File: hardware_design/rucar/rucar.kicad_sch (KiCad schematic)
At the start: 6 parts

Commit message: finish hardware design.
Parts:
- added D: D4, symbol Device:LED
- added D: RIGHT-FRONT, symbol Device:LED
- added D: D8, symbol Device:LED
- added D: D3, symbol Device:LED
- added D: LEFT-FRONT, symbol Device:LED
- added D: LEFT-BACK, symbol Device:LED
- added D: D7, symbol Device:LED
- added D: D1, symbol Device:LED
- added D: D2, symbol Device:LED
- added D: D5, symbol Device:LED
- added D: RIGHT-BACK, symbol Device:LED
- added D: D6, symbol Device:LED
- added LS?: Speaker, symbol Device:Speaker
- added R: 180k, symbol Device:R
- added U?: music_board_px85, symbol Audio:music_board_px85
- added U?: PS2_BOARD, symbol Device:PS2_BOARD
- MCU: value C8052RC -> C89C52RC
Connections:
- net GND: now also D.1 (K), D.1 (K), D.1 (K), D.1 (K), D.1 (K), D.1 (K), D.1 (K), D.1 (K), D.1 (K), D.1 (K), D.1 (K), D.1 (K), U?.3 (GND), U?.4 (GND)
- net at MCU.1 (P1.0/T2): now also D.2 (A)
- net at MCU.2 (P1.1/T2EX): now also D.2 (A)
- net at MCU.27 (P2.6/A14): now also U?.2 (~{C})
- net at MCU.3 (P1.2): now also D.2 (A)
- net at MCU.35 (P0.4/AD4): now also U?.7 (SCK/CLK)
- net at MCU.36 (P0.3/AD3): now also U?.2 (MIS/DO)
- net at MCU.37 (P0.2/AD2): now also U?.1 (MOS/DI)
- net at MCU.38 (P0.1/AD1): now also U?.6 (CS/SEL)
- net at MCU.4 (P1.3): now also D.2 (A)
- net at MCU.40 (VCC), U?.4 (Vs): now also U?.1 (VCC), U?.5 (VDD)
- net at MCU.5 (P1.4): now also D.2 (A)
- net at MCU.6 (P1.5): now also D.2 (A)
- net at MCU.7 (P1.6): now also D.2 (A)
- net at MCU.8 (P1.7): now also D.2 (A)
- new net: R.2, U?.4 (R2)
- new net: R.1, U?.5 (R1)
- new net: LS?.1, U?.7 (Out+)
- new net: LS?.2, U?.8 (Out-)
- new net: D.2 (A), D.2 (A), D.2 (A), D.2 (A)
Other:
- note added: "Marquee leds above the car"

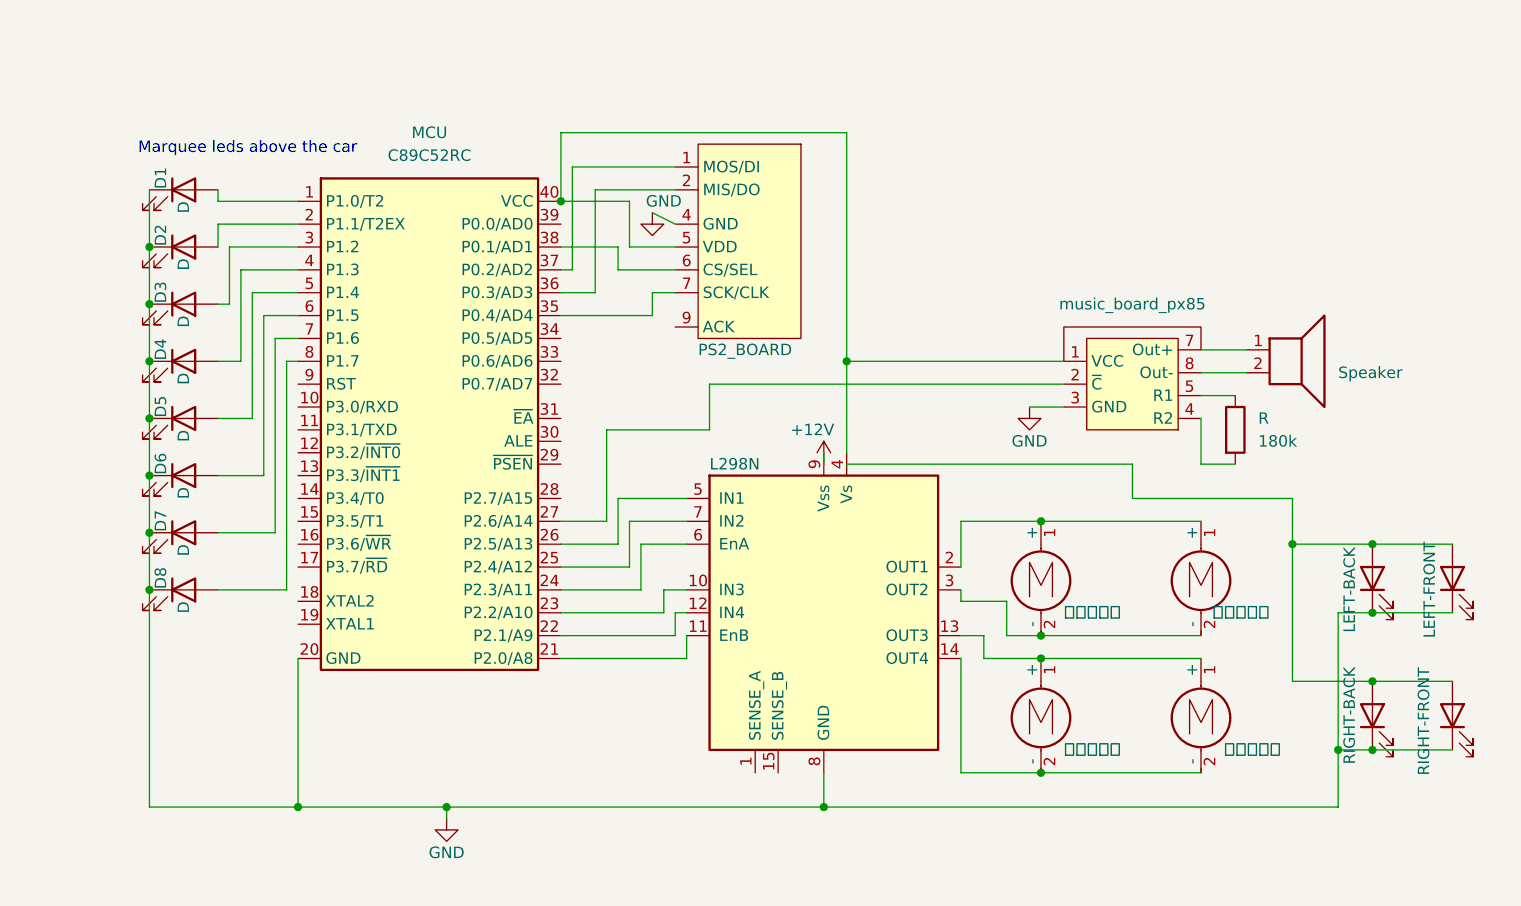
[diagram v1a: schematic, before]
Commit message: change ps2 gnio to P1
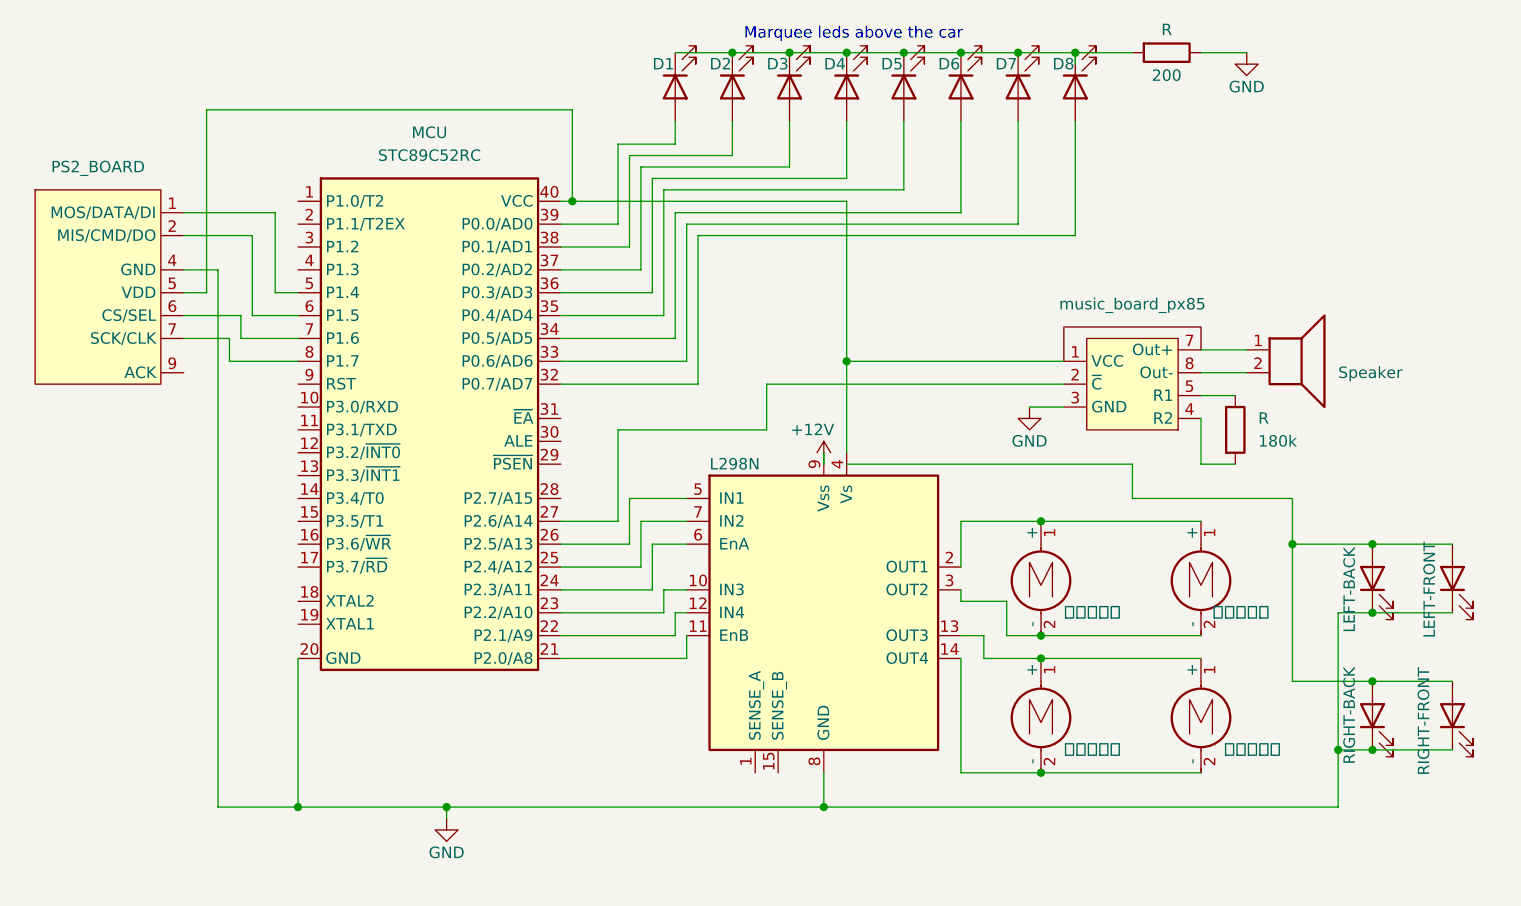
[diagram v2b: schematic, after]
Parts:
- removed U?: PS2_BOARD, symbol Device:PS2_BOARD
- added R: 200, symbol Device:R
- added U?: PS2_BOARD, symbol Device:PS2_BOARD
- MCU: value C89C52RC -> STC89C52RC
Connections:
- net GND: now also R.1, U?.4 (GND); no longer D.1 (K), D.1 (K), D.1 (K), D.1 (K), D.1 (K), D.1 (K), D.1 (K), D.1 (K)
- net at MCU.40 (VCC), U?.1 (VCC), U?.4 (Vs): now also U?.5 (VDD)
- net at MCU.1 (P1.0/T2): no longer D.2 (A)
- net at MCU.2 (P1.1/T2EX): no longer D.2 (A)
- net at MCU.3 (P1.2): no longer D.2 (A)
- net at MCU.32 (P0.7/AD7): now also D.2 (A)
- net at MCU.33 (P0.6/AD6): now also D.2 (A)
- net at MCU.34 (P0.5/AD5): now also D.2 (A)
- net at MCU.35 (P0.4/AD4): now also D.2 (A)
- net at MCU.36 (P0.3/AD3): now also D.2 (A)
- net at MCU.37 (P0.2/AD2): now also D.2 (A)
- net at MCU.38 (P0.1/AD1): now also D.2 (A)
- net at MCU.39 (P0.0/AD0): now also D.2 (A)
- net at MCU.4 (P1.3): no longer D.2 (A)
- net at MCU.5 (P1.4): now also U?.1 (MOS/DATA/DI); no longer D.2 (A)
- net at MCU.6 (P1.5): now also U?.2 (MIS/CMD/DO); no longer D.2 (A)
- net at MCU.7 (P1.6): now also U?.6 (CS/SEL); no longer D.2 (A)
- net at MCU.8 (P1.7): now also U?.7 (SCK/CLK); no longer D.2 (A)
- new net: D.1 (K), D.1 (K), D.1 (K), D.1 (K), D.1 (K), D.1 (K), D.1 (K), D.1 (K), R.2

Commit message: optimize
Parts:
- added Q: 2N3094, Package_TO_SOT_THT:TO-92_Inline, symbol Transistor_BJT:2N3904
- added Q?: 2N3094, Package_TO_SOT_THT:TO-39-3, symbol Transistor_BJT:2N2219
- added R? (x2): 5k, symbol Device:R
- added R? (x2): 2k, symbol Device:R
- added R?: 200, symbol Device:R
- D: value RIGHT-FRONT -> 右前
- D: value LEFT-FRONT -> 左前
- D: value LEFT-BACK -> 左后
- D: value RIGHT-BACK -> 右后
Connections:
- net GND: now also Q.1 (E), Q?.1 (E), R?.1, R?.1, R?.2; no longer D.1 (K), D.1 (K), D.1 (K), D.1 (K), U?.3 (GND)
- net at MCU.27 (P2.6/A14): now also R?.2; no longer U?.2 (~{C})
- net at MCU.28 (P2.7/A15): now also R?.1
- new net: Q.2 (B), R?.1, R?.1
- new net: Q?.2 (B), R?.2, R?.2
- new net: Q?.3 (C), U?.2 (~{C})
- new net: Q.3 (C), U?.3 (GND)
- new net: D.1 (K), D.1 (K), D.1 (K), D.1 (K), R?.2
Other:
- note added: "Leds of car"
- moved on the sheet: R
